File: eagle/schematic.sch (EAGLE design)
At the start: 19 parts, among them Q3 TIP120, Q4 TIP120, T1 2N3904, T2 2N3904

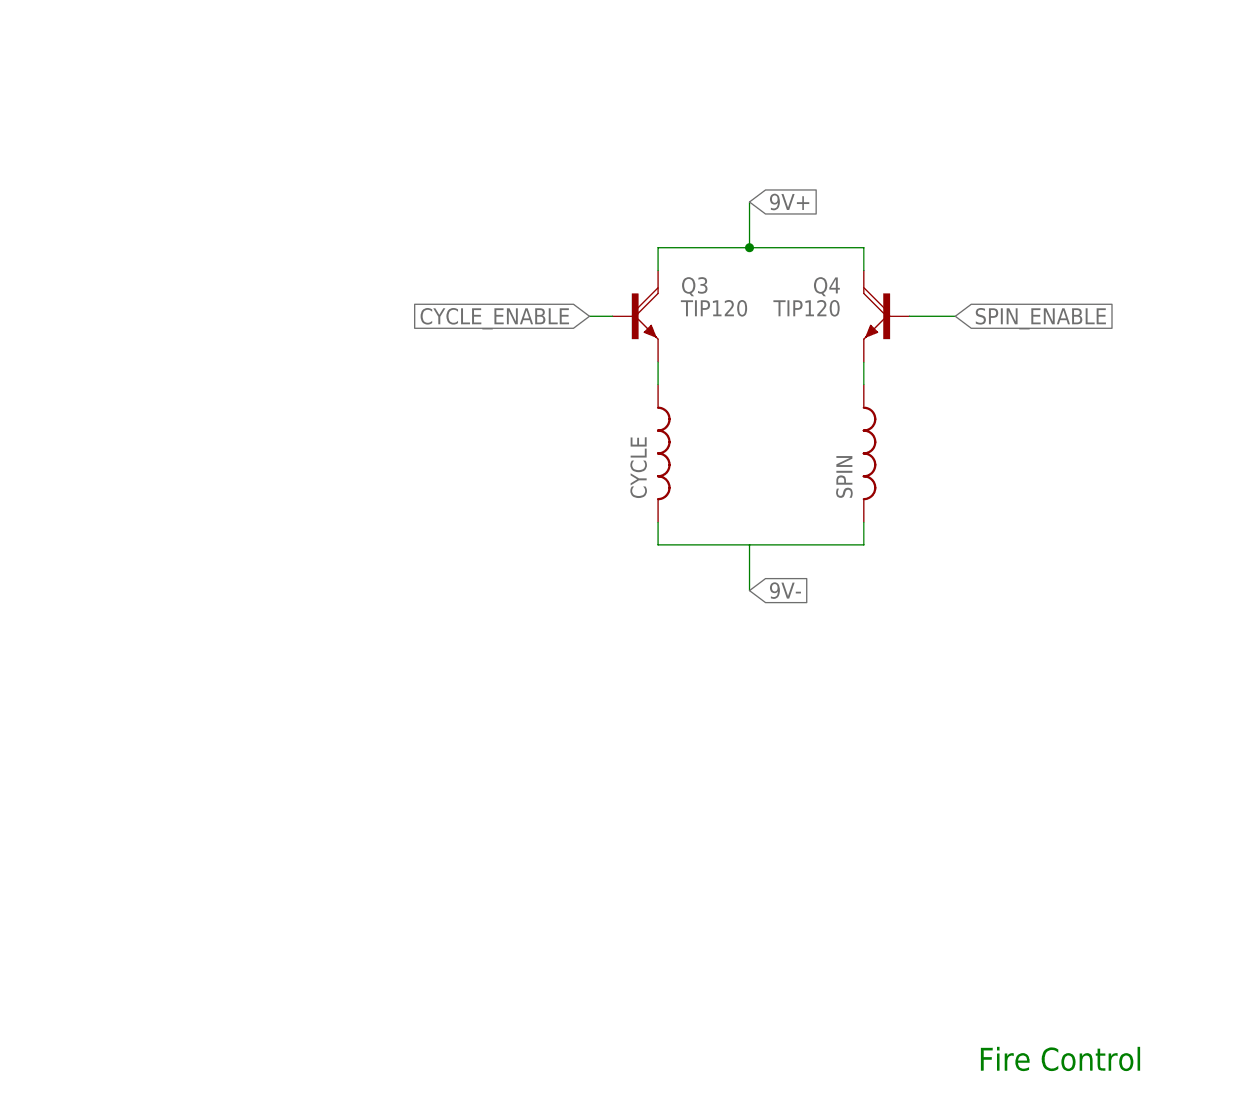
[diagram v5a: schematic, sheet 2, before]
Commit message: Replacing TIP120s with N-Channel MOSFETs
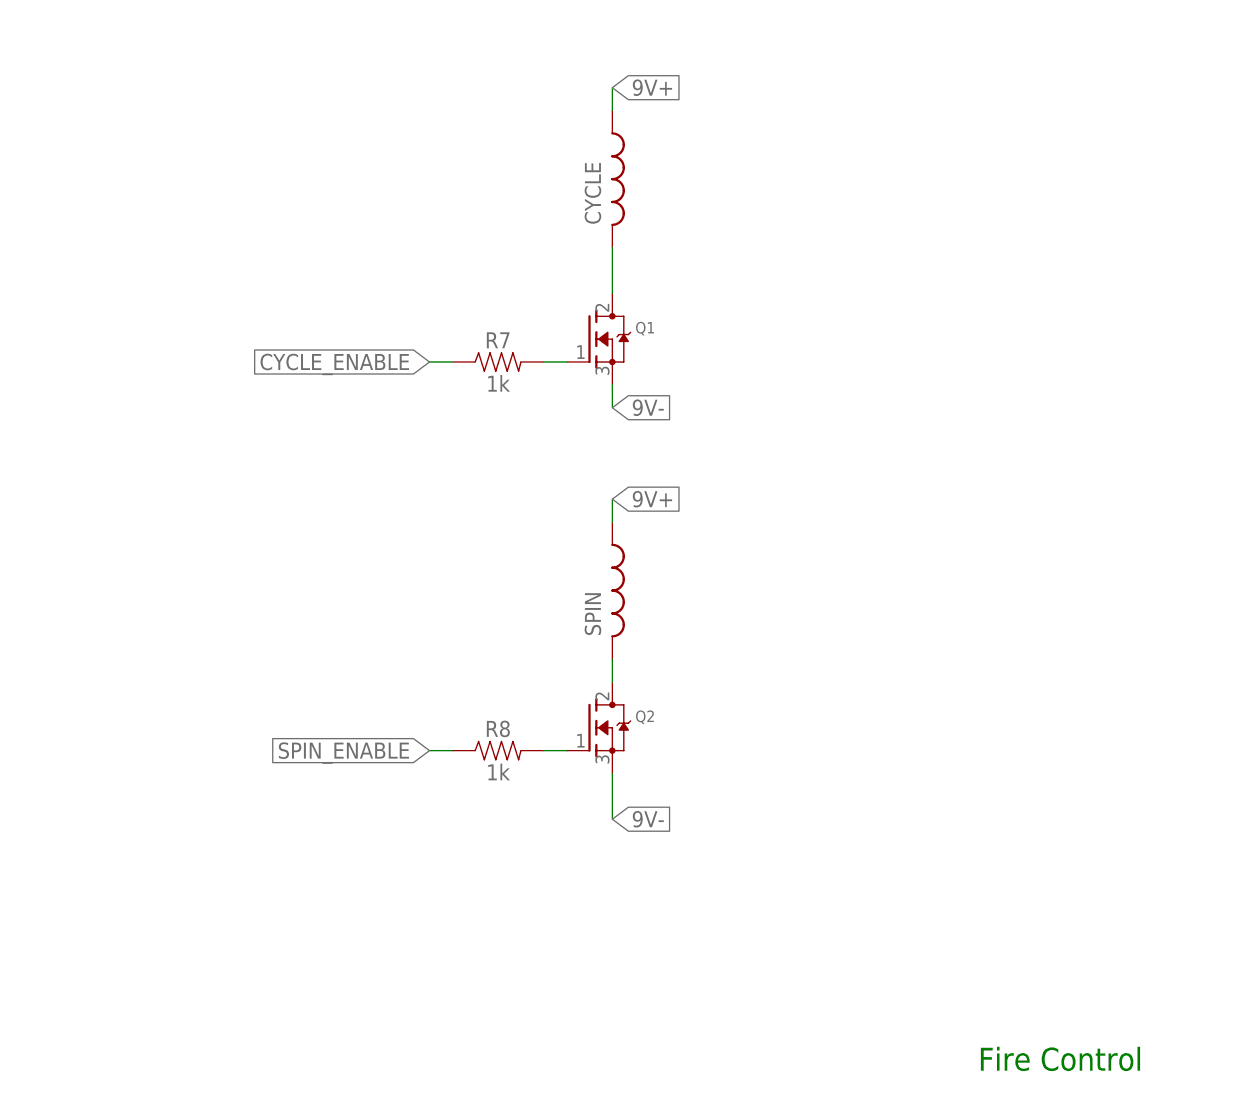
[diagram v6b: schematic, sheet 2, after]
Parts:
- removed Q3, Q4: TIP120, transistor-power:TIP120
- added Q1, Q2: (no value), adafruit:MOSFET-NGDS_TO220V
- added R7, R8: 1k, SparkFun-Resistors:1KOHM-HORIZ-1/4W-5%
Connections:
- removed net N$6: Q4.E, SPIN.1
- new net N$1: CYCLE.2, Q1.D
- new net N$2: Q2.D, SPIN.2
- net 9V+: now also CYCLE.1, SPIN.1; no longer Q3.C, Q4.C
- net 9V-: now also Q1.S, Q2.S; no longer CYCLE.2, SPIN.2
- net CYCLE_ENABLE: now also R7.1; no longer Q3.B
- net N$5: now also Q1.G, R7.2; no longer CYCLE.1, Q3.E
- net SPIN_ENABLE: now also Q2.G, R8.1, R8.2; no longer Q4.B
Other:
- moved on the sheet: CYCLE, SPIN
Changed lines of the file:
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@@
 <part name="R3" library="SparkFun-Resistors" deviceset="1KOHM" device="-HORIZ-1/4W-1%" value="1k"/>
 <part name="R4" library="SparkFun-Resistors" deviceset="1KOHM" device="-HORIZ-1/4W-1%" value="1k"/>
-<part name="Q3" library="transistor-power" library_urn="urn:adsk.eagle:library:400" deviceset="TIP120" device="" package3d_urn="urn:adsk.eagle:package:29488/1"/>
-<part name="Q4" library="transistor-power" library_urn="urn:adsk.eagle:library:400" deviceset="TIP120" device="" package3d_urn="urn:adsk.eagle:package:29488/1"/>
 <part name="SPIN" library="rcl" library_urn="urn:adsk.eagle:library:334" deviceset="L-US" device="0204/5" package3d_urn="urn:adsk.eagle:package:23488/1"/>
 <part name="CYCLE" library="rcl" library_urn="urn:adsk.eagle:library:334" deviceset="L-US" device="0204/5" package3d_urn="urn:adsk.eagle:package:23488/1"/>
@@
 <part name="R5" library="SparkFun-Resistors" deviceset="1KOHM" device="-HORIZ-1/4W-1%" value="4.7k"/>
 <part name="R6" library="SparkFun-Resistors" deviceset="1KOHM" device="-HORIZ-1/4W-1%" value="10k"/>
+<part name="Q1" library="adafruit" library_urn="urn:adsk.eagle:library:420" deviceset="MOSFET-N" device="GDS_TO220V" package3d_urn="urn:adsk.eagle:package:6240882/1"/>
+<part name="Q2" library="adafruit" library_urn="urn:adsk.eagle:library:420" deviceset="MOSFET-N" device="GDS_TO220V" package3d_urn="urn:adsk.eagle:package:6240882/1"/>
+<part name="R7" library="SparkFun-Resistors" library_urn="urn:adsk.eagle:library:532" deviceset="1KOHM" device="-HORIZ-1/4W-5%" package3d_urn="urn:adsk.eagle:package:39658/1" value="1k"/>
+<part name="R8" library="SparkFun-Resistors" library_urn="urn:adsk.eagle:library:532" deviceset="1KOHM" device="-HORIZ-1/4W-5%" package3d_urn="urn:adsk.eagle:package:39658/1" value="1k"/>
 </parts>
 <sheets>
@@
 </plain>
 <instances>
-<instance part="Q3" gate="1" x="0" y="78.74">
-<attribute name="NAME" x="5.08" y="81.28" size="1.778" layer="95"/>
-<attribute name="VALUE" x="5.08" y="78.74" size="1.778" layer="96"/>
-</instance>
-<instance part="Q4" gate="1" x="27.94" y="78.74" rot="MR0">
-<attribute name="NAME" x="22.86" y="81.28" size="1.778" layer="95" rot="MR0"/>
-<attribute name="VALUE" x="22.86" y="78.74" size="1.778" layer="96" rot="MR0"/>
-</instance>
-<instance part="SPIN" gate="G$1" x="25.4" y="63.5">
-<attribute name="NAME" x="24.13" y="58.42" size="1.778" layer="95" rot="R90"/>
-<attribute name="VALUE" x="29.21" y="58.42" size="1.778" layer="96" rot="R90"/>
-</instance>
-<instance part="CYCLE" gate="G$1" x="2.54" y="63.5">
-<attribute name="NAME" x="1.27" y="58.42" size="1.778" layer="95" rot="R90"/>
-<attribute name="VALUE" x="6.35" y="58.42" size="1.778" layer="96" rot="R90"/>
+<instance part="SPIN" gate="G$1" x="-2.54" y="48.26">
+<attribute name="NAME" x="-3.81" y="43.18" size="1.778" layer="95" rot="R90"/>
+<attribute name="VALUE" x="1.27" y="43.18" size="1.778" layer="96" rot="R90"/>
+</instance>
+<instance part="CYCLE" gate="G$1" x="-2.54" y="93.98">
+<attribute name="NAME" x="-3.81" y="88.9" size="1.778" layer="95" rot="R90"/>
+<attribute name="VALUE" x="1.27" y="88.9" size="1.778" layer="96" rot="R90"/>
 </instance>
 <instance part="FRAME2" gate="G$1" x="-121.92" y="-22.86"/>
@@
 <attribute name="SHEET" x="111.76" y="-21.59" size="2.54" layer="94"/>
 </instance>
+<instance part="Q1" gate="G$1" x="-5.08" y="76.2">
+<attribute name="NAME" x="0" y="76.835" size="1.27" layer="95"/>
+<attribute name="VALUE" x="0" y="74.93" size="1.27" layer="96"/>
+</instance>
+<instance part="Q2" gate="G$1" x="-5.08" y="33.02">
+<attribute name="NAME" x="0" y="33.655" size="1.27" layer="95"/>
+<attribute name="VALUE" x="0" y="31.75" size="1.27" layer="96"/>
+</instance>
+<instance part="R7" gate="G$1" x="-15.24" y="73.66">
+<attribute name="NAME" x="-15.24" y="75.184" size="1.778" layer="95" font="vector" align="bottom-center"/>
+<attribute name="VALUE" x="-15.24" y="72.136" size="1.778" layer="96" font="vector" align="top-center"/>
+</instance>
+<instance part="R8" gate="G$1" x="-15.24" y="30.48">
+<attribute name="NAME" x="-15.24" y="32.004" size="1.778" layer="95" font="vector" align="bottom-center"/>
+<attribute name="VALUE" x="-15.24" y="28.956" size="1.778" layer="96" font="vector" align="top-center"/>
+</instance>
 </instances>
 <busses>
 </busses>
 <nets>
+<net name="9V-" class="0">
+<segment>
+<pinref part="Q2" gate="G$1" pin="S"/>
+<wire x1="-2.54" y1="22.86" x2="-2.54" y2="27.94" width="0.1524" layer="91"/>
+<label x="-2.54" y="22.86" size="1.778" layer="95" xref="yes"/>
+</segment>
+<segment>
+<pinref part="Q1" gate="G$1" pin="S"/>
+<wire x1="-2.54" y1="68.58" x2="-2.54" y2="71.12" width="0.1524" layer="91"/>
+<label x="-2.54" y="68.58" size="1.778" layer="95" xref="yes"/>
+</segment>
+</net>
+<net name="SPIN_ENABLE" class="0">
+<segment>
+<wire x1="-7.62" y1="30.48" x2="-10.16" y2="30.48" width="0.1524" layer="91"/>
+<pinref part="Q2" gate="G$1" pin="G"/>
+<pinref part="R8" gate="G$1" pin="2"/>
+</segment>
+<segment>
+<pinref part="R8" gate="G$1" pin="1"/>
+<wire x1="-20.32" y1="30.48" x2="-22.86" y2="30.48" width="0.1524" layer="91"/>
+<label x="-22.86" y="30.48" size="1.778" layer="95" rot="R180" xref="yes"/>
+</segment>
+</net>
+<net name="N$1" class="0">
+<segment>
+<pinref part="CYCLE" gate="G$1" pin="2"/>
+<pinref part="Q1" gate="G$1" pin="D"/>
+<wire x1="-2.54" y1="86.36" x2="-2.54" y2="81.28" width="0.1524" layer="91"/>
+</segment>
+</net>
+<net name="N$2" class="0">
+<segment>
+<pinref part="SPIN" gate="G$1" pin="2"/>
+<pinref part="Q2" gate="G$1" pin="D"/>
+<wire x1="-2.54" y1="40.64" x2="-2.54" y2="38.1" width="0.1524" layer="91"/>
+</segment>
+</net>
 <net name="N$5" class="0">
 <segment>
-<pinref part="Q3" gate="1" pin="E"/>
+<pinref part="Q1" gate="G$1" pin="G"/>
+<pinref part="R7" gate="G$1" pin="2"/>
+<wire x1="-7.62" y1="73.66" x2="-10.16" y2="73.66" width="0.1524" layer="91"/>
+</segment>
+</net>
+<net name="CYCLE_ENABLE" class="0">
+<segment>
+<pinref part="R7" gate="G$1" pin="1"/>
+<wire x1="-22.86" y1="73.66" x2="-20.32" y2="73.66" width="0.1524" layer="91"/>
+<label x="-22.86" y="73.66" size="1.778" layer="95" rot="R180" xref="yes"/>
+</segment>
+</net>
+<net name="9V+" class="0">
+<segment>
+<pinref part="SPIN" gate="G$1" pin="1"/>
+<wire x1="-2.54" y1="58.42" x2="-2.54" y2="55.88" width="0.1524" layer="91"/>
+<label x="-2.54" y="58.42" size="1.778" layer="95" xref="yes"/>
+</segment>
+<segment>
 <pinref part="CYCLE" gate="G$1" pin="1"/>
-<wire x1="2.54" y1="73.66" x2="2.54" y2="71.12" width="0.1524" layer="91"/>
-</segment>
-</net>
-<net name="N$6" class="0">
-<segment>
-<pinref part="Q4" gate="1" pin="E"/>
-<pinref part="SPIN" gate="G$1" pin="1"/>
-<wire x1="25.4" y1="73.66" x2="25.4" y2="71.12" width="0.1524" layer="91"/>
-</segment>
-</net>
-<net name="9V+" class="0">
-<segment>
-<pinref part="Q3" gate="1" pin="C"/>
-<wire x1="2.54" y1="86.36" x2="2.54" y2="83.82" width="0.1524" layer="91"/>
-<pinref part="Q4" gate="1" pin="C"/>
-<wire x1="2.54" y1="86.36" x2="12.7" y2="86.36" width="0.1524" layer="91"/>
-<wire x1="12.7" y1="86.36" x2="25.4" y2="86.36" width="0.1524" layer="91"/>
-<wire x1="25.4" y1="86.36" x2="25.4" y2="83.82" width="0.1524" layer="91"/>
-<wire x1="12.7" y1="86.36" x2="12.7" y2="91.44" width="0.1524" layer="91"/>
-<junction x="12.7" y="86.36"/>
-<label x="12.7" y="91.44" size="1.778" layer="95" xref="yes"/>
-</segment>
-</net>
-<net name="9V-" class="0">
-<segment>
-<pinref part="CYCLE" gate="G$1" pin="2"/>
-<wire x1="2.54" y1="55.88" x2="2.54" y2="53.34" width="0.1524" layer="91"/>
-<wire x1="2.54" y1="53.34" x2="12.7" y2="53.34" width="0.1524" layer="91"/>
-<pinref part="SPIN" gate="G$1" pin="2"/>
-<wire x1="12.7" y1="53.34" x2="25.4" y2="53.34" width="0.1524" layer="91"/>
-<wire x1="25.4" y1="53.34" x2="25.4" y2="55.88" width="0.1524" layer="91"/>
-<wire x1="12.7" y1="53.34" x2="12.7" y2="48.26" width="0.1524" layer="91"/>
-<label x="12.7" y="48.26" size="1.778" layer="95" xref="yes"/>
-</segment>
-</net>
-<net name="SPIN_ENABLE" class="0">
-<segment>
-<pinref part="Q4" gate="1" pin="B"/>
-<wire x1="30.48" y1="78.74" x2="35.56" y2="78.74" width="0.1524" layer="91"/>
-<label x="35.56" y="78.74" size="1.778" layer="95" xref="yes"/>
-</segment>
-</net>
-<net name="CYCLE_ENABLE" class="0">
-<segment>
-<pinref part="Q3" gate="1" pin="B"/>
-<wire x1="-2.54" y1="78.74" x2="-5.08" y2="78.74" width="0.1524" layer="91"/>
-<label x="-5.08" y="78.74" size="1.778" layer="95" rot="R180" xref="yes"/>
-</segment>
-</net>
+<wire x1="-2.54" y1="101.6" x2="-2.54" y2="104.14" width="0.1524" layer="91"/>
+<label x="-2.54" y="104.14" size="1.778" layer="95" xref="yes"/>
+</segment>
+</net>

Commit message: Adding dedicated flyback diode to spin / cycle circuit
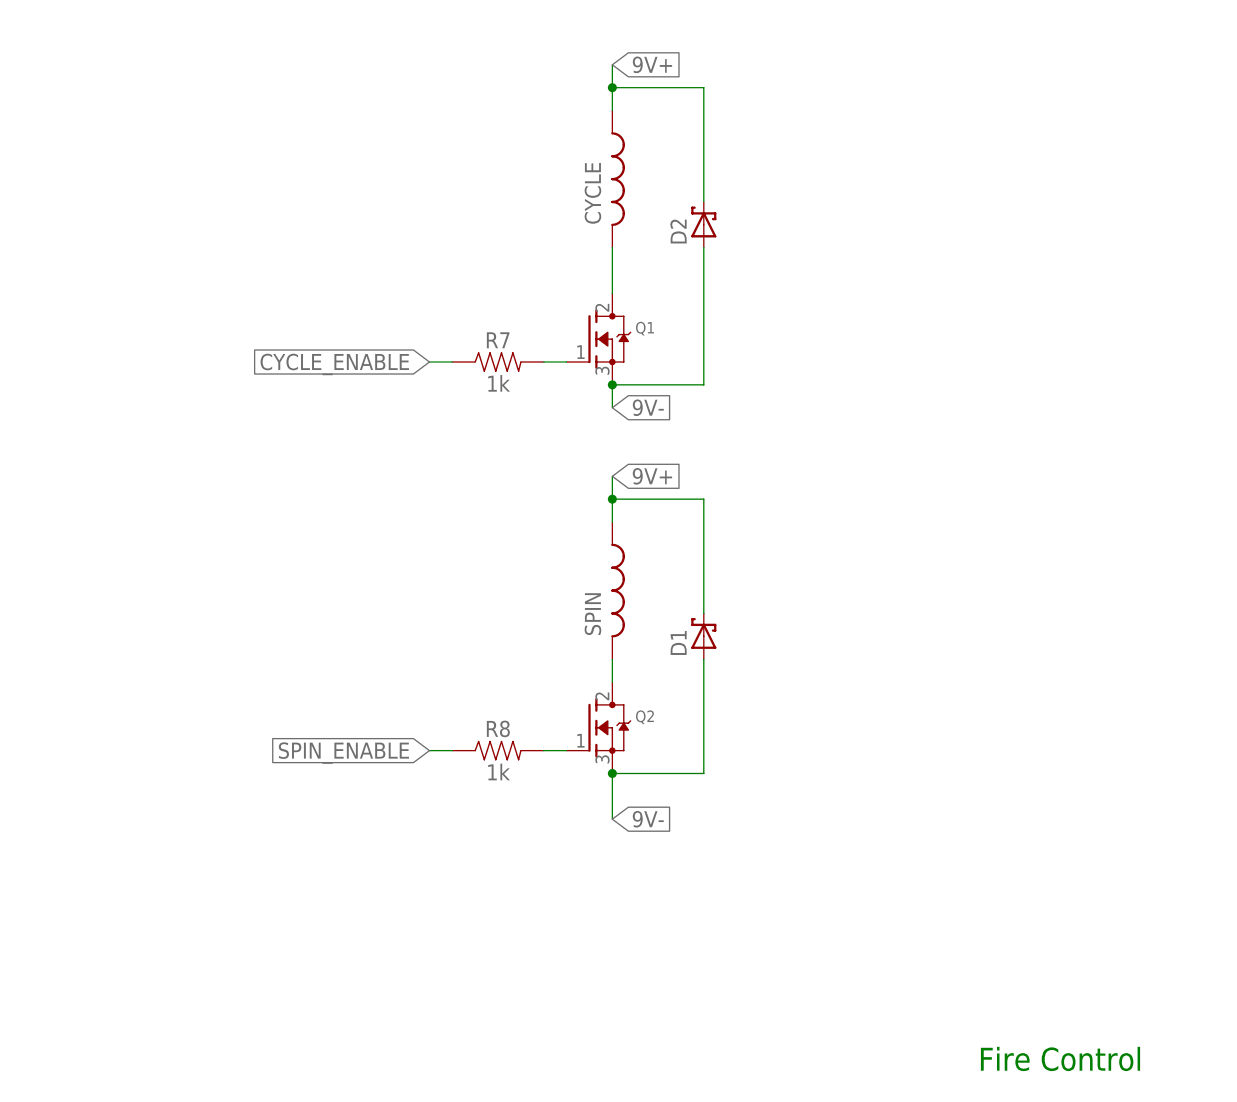
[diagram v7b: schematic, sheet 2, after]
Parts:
- added D1, D2: (no value), adafruit:SCHOTTKY-DIODECB417-15
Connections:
- net 9V+: now also D1.C, D2.C
- net 9V-: now also D1.A, D2.A
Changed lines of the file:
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@@
 <part name="R7" library="SparkFun-Resistors" library_urn="urn:adsk.eagle:library:532" deviceset="1KOHM" device="-HORIZ-1/4W-5%" package3d_urn="urn:adsk.eagle:package:39658/1" value="1k"/>
 <part name="R8" library="SparkFun-Resistors" library_urn="urn:adsk.eagle:library:532" deviceset="1KOHM" device="-HORIZ-1/4W-5%" package3d_urn="urn:adsk.eagle:package:39658/1" value="1k"/>
+<part name="D1" library="adafruit" library_urn="urn:adsk.eagle:library:420" deviceset="SCHOTTKY-DIODE" device="CB417-15" package3d_urn="urn:adsk.eagle:package:6240685/1"/>
+<part name="D2" library="adafruit" library_urn="urn:adsk.eagle:library:420" deviceset="SCHOTTKY-DIODE" device="CB417-15" package3d_urn="urn:adsk.eagle:package:6240685/1"/>
 </parts>
 <sheets>
@@
 <attribute name="VALUE" x="-15.24" y="28.956" size="1.778" layer="96" font="vector" align="top-center"/>
 </instance>
+<instance part="D1" gate="G$1" x="7.62" y="43.18" rot="R90">
+<attribute name="NAME" x="5.715" y="40.894" size="1.778" layer="95" rot="R90"/>
+<attribute name="VALUE" x="11.049" y="40.894" size="1.778" layer="96" rot="R90"/>
+</instance>
+<instance part="D2" gate="G$1" x="7.62" y="88.9" rot="R90">
+<attribute name="NAME" x="5.715" y="86.614" size="1.778" layer="95" rot="R90"/>
+<attribute name="VALUE" x="11.049" y="86.614" size="1.778" layer="96" rot="R90"/>
+</instance>
 </instances>
 <busses>
@@
 <wire x1="-2.54" y1="22.86" x2="-2.54" y2="27.94" width="0.1524" layer="91"/>
 <label x="-2.54" y="22.86" size="1.778" layer="95" xref="yes"/>
+<wire x1="-2.54" y1="27.94" x2="7.62" y2="27.94" width="0.1524" layer="91"/>
+<junction x="-2.54" y="27.94"/>
+<pinref part="D1" gate="G$1" pin="A"/>
+<wire x1="7.62" y1="27.94" x2="7.62" y2="40.64" width="0.1524" layer="91"/>
 </segment>
 <segment>
@@
 <wire x1="-2.54" y1="68.58" x2="-2.54" y2="71.12" width="0.1524" layer="91"/>
 <label x="-2.54" y="68.58" size="1.778" layer="95" xref="yes"/>
+<wire x1="-2.54" y1="71.12" x2="7.62" y2="71.12" width="0.1524" layer="91"/>
+<junction x="-2.54" y="71.12"/>
+<pinref part="D2" gate="G$1" pin="A"/>
+<wire x1="7.62" y1="71.12" x2="7.62" y2="86.36" width="0.1524" layer="91"/>
 </segment>
 </net>
@@
 <segment>
 <pinref part="SPIN" gate="G$1" pin="1"/>
+<wire x1="-2.54" y1="60.96" x2="-2.54" y2="58.42" width="0.1524" layer="91"/>
+<label x="-2.54" y="60.96" size="1.778" layer="95" xref="yes"/>
+<pinref part="D1" gate="G$1" pin="C"/>
 <wire x1="-2.54" y1="58.42" x2="-2.54" y2="55.88" width="0.1524" layer="91"/>
-<label x="-2.54" y="58.42" size="1.778" layer="95" xref="yes"/>
+<wire x1="7.62" y1="45.72" x2="7.62" y2="58.42" width="0.1524" layer="91"/>
+<wire x1="7.62" y1="58.42" x2="-2.54" y2="58.42" width="0.1524" layer="91"/>
+<junction x="-2.54" y="58.42"/>
+</segment>
+<segment>
+<pinref part="D2" gate="G$1" pin="C"/>
+<wire x1="7.62" y1="91.44" x2="7.62" y2="104.14" width="0.1524" layer="91"/>
+<junction x="-2.54" y="104.14"/>
+<wire x1="7.62" y1="104.14" x2="-2.54" y2="104.14" width="0.1524" layer="91"/>
 </segment>
 <segment>
 <pinref part="CYCLE" gate="G$1" pin="1"/>
-<wire x1="-2.54" y1="101.6" x2="-2.54" y2="104.14" width="0.1524" layer="91"/>
-<label x="-2.54" y="104.14" size="1.778" layer="95" xref="yes"/>
-</segment>
-</net>
+<wire x1="-2.54" y1="101.6" x2="-2.54" y2="106.68" width="0.1524" layer="91"/>
+<label x="-2.54" y="106.68" size="1.778" layer="95" xref="yes"/>
+</segment>
+</net>
